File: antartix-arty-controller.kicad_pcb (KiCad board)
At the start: 2 copper layers, 68.5 x 40 mm, 103 parts, among them IC1 FT2232D, J1 QTE-020-04-L-D-A, J2 614004185023, J3 614004185023, J4 614004185023, J5 WE_629105150521, U1 PCT2075GVX, U2 PAC1934T-I_JQ, U3 USB2514B-I_M2, U4 TPS2024DR, U5 TPS2024DR, U6 TPS2024DR, U7 TPS2051BDBVR, Y1 7C-24.000MBB-T, Y2 MQ-6.000-12-30_30_

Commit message: Layout done
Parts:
- C31: moved to F.Cu
- C7, U2: moved to B.Cu
- moved N1 71.2 mm to (169.6, 89.1)
- moved C31 49.5 mm to (147.9, 61.0)
- moved N2 33.4 mm to (144.8, 72.3)
- moved C33 29.3 mm to (155.0, 61.3)
- moved C37 29.3 mm to (153.8, 61.1)
- moved U7 29.2 mm to (150.8, 60.8)
- moved D4 16.4 mm to (113.8, 77.2)
- moved R10 16.4 mm to (110.9, 80.4)
- moved R12 16.4 mm to (110.9, 77.2)
- moved D2 16.4 mm to (113.8, 80.4)
- moved D3 16.4 mm to (113.8, 82.1)
- moved D5 16.4 mm to (113.8, 78.8)
- moved R11 16.4 mm to (110.9, 82.1)
- moved R13 16.4 mm to (110.9, 78.8)
- moved C36 4.55 mm to (118.8, 77.9)
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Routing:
- net VBUS1: track 33.7 -> 16.2 mm, vias 2 -> 1
- net VBUS1_S: track 21.6 -> 4.82 mm, vias 3 -> 2
- net VBUS4_S: track 2.87 -> 15.8 mm
- net VBUS3: track 31.3 -> 29.5 mm, vias 2 -> 1
- net VBUS3_S: track 23.4 -> 22.2 mm, vias 2 -> 1
- net VBUS2_S: track 7.28 -> 8.10 mm, vias 0 -> 1
- net VBUS2: track 17.9 -> 18.6 mm, vias 0 -> 1

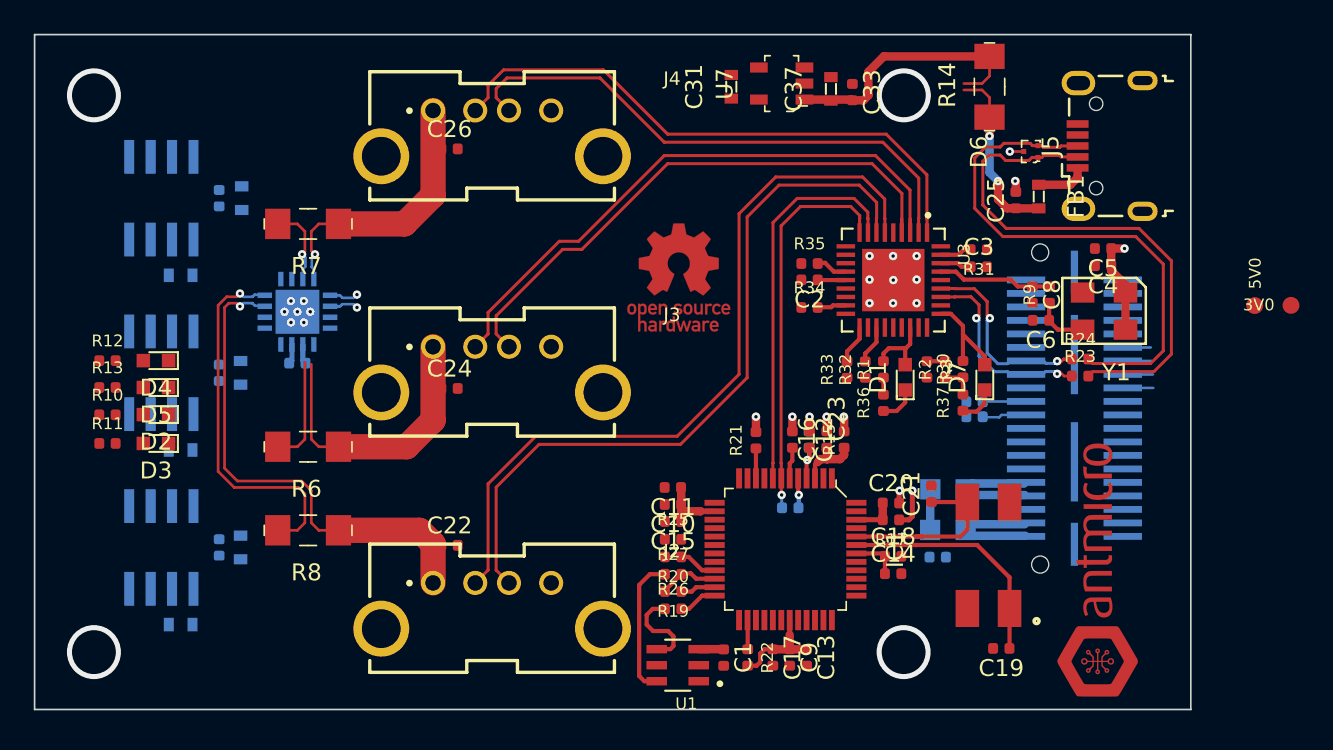
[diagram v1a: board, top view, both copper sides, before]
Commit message: Routing control signals
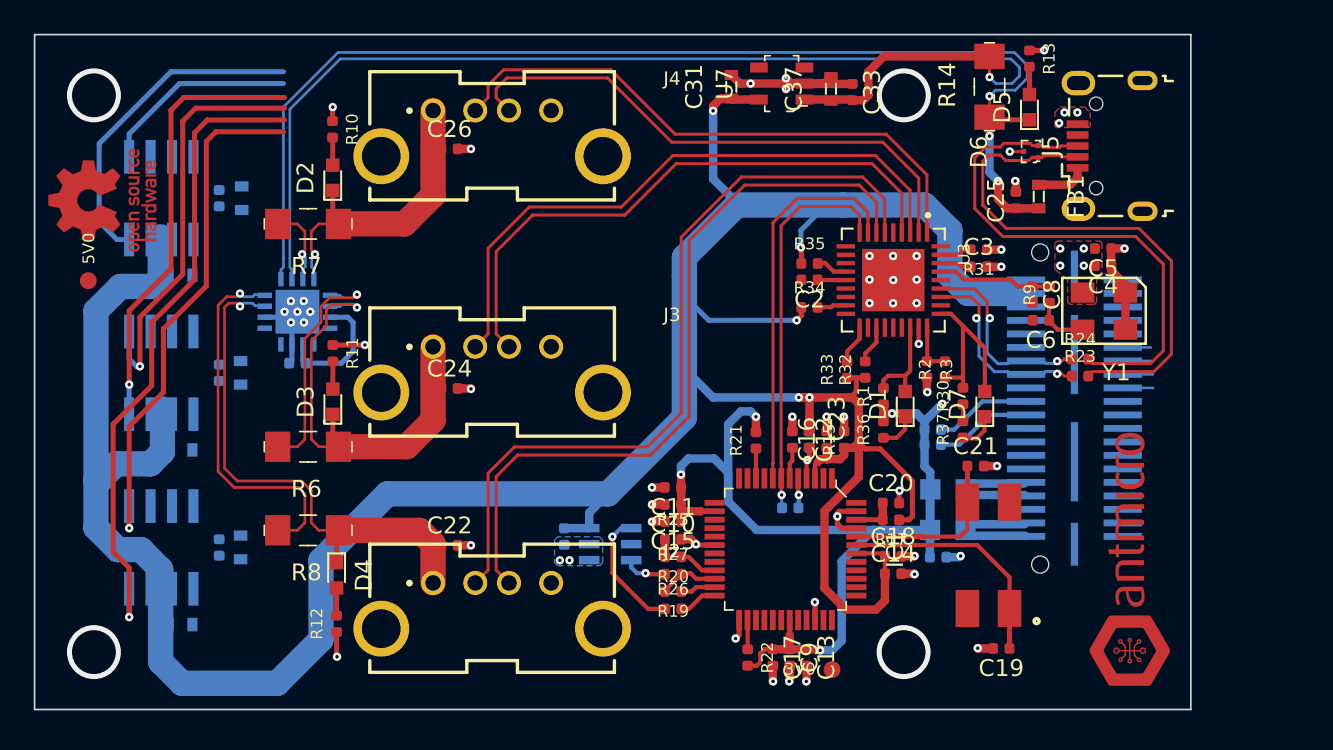
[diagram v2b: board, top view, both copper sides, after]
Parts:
- C1, U1: moved to B.Cu
- moved 5V0 69.1 mm to (109.7, 72.4)
- moved R13 58.0 mm to (165.5, 59.3), turned to 270 degrees
- moved D5 54.4 mm to (165.5, 62.2), turned to 90 degrees
- moved 3V0 34.7 mm to (153.8, 95.5)
- moved N2 34.5 mm to (110.6, 67.7), turned to 90 degrees
- moved R10 21.5 mm to (124.2, 63.5), turned to 270 degrees
- moved R12 20.7 mm to (124.5, 92.8), turned to 90 degrees
- moved D2 17.5 mm to (124.2, 66.3), turned to 90 degrees
- moved D4 16.6 mm to (124.5, 89.9), turned to 270 degrees
- moved R11 14.4 mm to (124.2, 76.7), turned to 270 degrees
- moved C1 11.9 mm to (138.0, 87.6)
- moved D3 10.8 mm to (124.2, 79.6), turned to 90 degrees
- moved U1 8.22 mm to (140.7, 88.1), turned to 0 degrees
- moved C21 3.09 mm to (162.3, 83.4), turned to 0 degrees
- moved R4 2.98 mm to (159.8, 81.3)
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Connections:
- D2 pad 1: VBUS1_S -> VBUS1
- D3 pad 1: VBUS2_S -> VBUS2
- D4 pad 1: VBUS3_S -> VBUS3
- D5 pad 1: VBUS4_S -> VBUS4
- U2 pad 17: (no net) -> GND
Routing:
- net VCC5V0: track 12.5 -> 201.7 mm, vias 2 -> 5
- net VBUS4: track 10.6 -> 70.8 mm, vias 2 -> 3
- net VBUS4_S: track 15.8 -> 72.7 mm, vias 0 -> 1
- net VCC3V3: track 22.3 -> 69.9 mm, vias 2 -> 6
- net GND: track 6.01 -> 46.1 mm, vias 15 -> 59
- net /USB3_EN: track 1.81 -> 40.2 mm, vias 0 -> 1
- net /OC_N3: track 2.31 -> 33.2 mm, vias 0 -> 1
- net /USB2_EN: track 1.79 -> 27.9 mm, vias 0 -> 1
- net /OC_N2: track 1.67 -> 26.1 mm, vias 0 -> 1
- net /USB1_EN: track 1.71 -> 21.2 mm
- net /OC_N1: track 1.85 -> 13.6 mm
- net VBUS2: track 18.6 -> 26.3 mm
- net VBUS2_S: track 8.10 -> 14.2 mm
- net SCL0: track 7.93 -> 13.2 mm, vias 0 -> 1
- net /SUSP_IND: track 6.02 -> 9.69 mm
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- added copper zone on B.Cu, net GND
- added copper zone on F.Cu, net GND
- added copper zone on In1.Cu, net GND
- added copper zone on In2.Cu, net GND
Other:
- copper layers 2 -> 4

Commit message: Board routed
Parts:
- added C40: C_1u_0402, antmicro-footprints:0402-cap, F.Cu at (165.8, 78.7)
- added C41: C_100n_0402, antartix-arty-controller-footprints:0402-cap, B.Cu at (157.5, 69.8)
- added C42: C_100n_0402, antartix-arty-controller-footprints:0402-cap, B.Cu at (160.2, 70.9)
- added C43: C_100n_0402, antartix-arty-controller-footprints:0402-cap, B.Cu at (154.9, 70.3)
- added C44: C_100n_0402, antartix-arty-controller-footprints:0402-cap, B.Cu at (160.2, 73.9)
- added C45: C_100n_0402, antartix-arty-controller-footprints:0402-cap, B.Cu at (154.9, 72.9)
- added C46: C_100n_0402, antartix-arty-controller-footprints:0402-cap, B.Cu at (157.5, 75.2)
- added C47: C_330u_KEMET_D, antmicro-footprints:KEMET_D, B.Cu at (133.7, 66.0)
- added C48: C_330u_KEMET_D, antmicro-footprints:KEMET_D, B.Cu at (133.7, 79.9)
- added C49: C_330u_KEMET_D, antmicro-footprints:KEMET_D, B.Cu at (133.7, 94.1)
- added C50: C_680u_KEMET_D, antmicro-footprints:KEMET_D, B.Cu at (123.5, 87.0)
- added GND: TP_SMD1MM, antartix-arty-controller-footprints:Testpoint_smd_1mm, F.Cu at (107.6, 74.3)
- added GND: TP_SMD1MM, antartix-arty-controller-footprints:Testpoint_smd_1mm, F.Cu at (170.7, 90.4)
- moved N1 61.5 mm to (110.2, 84.1)
- moved R4 18.7 mm to (144.4, 91.9), turned to 0 degrees
- moved R5 17.2 mm to (144.4, 89.8), turned to 180 degrees
- moved 3V0 15.3 mm to (168.2, 90.5)
- moved C26 4.93 mm to (130.1, 69.5)
- moved C24 3.94 mm to (130.1, 82.6)
- moved C36 3.22 mm to (118.3, 81.1), turned to 0 degrees
- moved R9 2.42 mm to (164.6, 74.5)
- moved C32 2.05 mm to (118.3, 79.8), turned to 0 degrees
- moved 5V0 1.88 mm to (109.3, 74.3)
- moved C4 1.14 mm to (168.8, 71.6)
- moved C5 1.14 mm to (168.8, 70.5)
- moved Y1 1.14 mm to (169.1, 74.0)
- moved C22 0.90 mm to (131.0, 87.2)
- moved D6 0.84 mm to (165.9, 64.0)
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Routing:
- net /USB1_EN: track 21.2 -> 157.3 mm, vias 0 -> 5
- net /USB2_EN: track 27.9 -> 160.6 mm, vias 1 -> 7
- net VCC3V3: track 69.9 -> 172.2 mm, vias 6 -> 15
- net /USB3_EN: track 40.2 -> 112.5 mm, vias 1 -> 3
- net SDA0: track 8.37 -> 73.2 mm, vias 1 -> 5
- net /SLOW_~ALERT: track 0.00 -> 59.6 mm, vias 0 -> 4
- net SCL0: track 13.2 -> 71.2 mm, vias 1 -> 4
- net /~PWRDN: track 0.00 -> 57.9 mm, vias 0 -> 4
- net VCC5V0: track 201.7 -> 251.2 mm, vias 5 -> 10
- net /OC_N1: track 13.6 -> 53.1 mm, vias 0 -> 5
- net /OC_N3: track 33.2 -> 68.9 mm, vias 1 -> 5
- net /OC_N2: track 26.1 -> 59.3 mm, vias 1 -> 5
- net /USB4_EN: track 0.00 -> 32.3 mm, vias 0 -> 4
- net /OC_N4: track 2.28 -> 33.1 mm, vias 0 -> 4
- net GND: track 46.1 -> 66.8 mm, vias 59 -> 95
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- added copper zone on B.Cu, net VBUS1_S
- added copper zone on B.Cu, net VBUS2_S
- added copper zone on B.Cu, net VBUS3_S
- added copper zone on F.Cu, net VCC3V3
- added copper zone on B.Cu, net VCC5V0
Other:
- board text added: "Rev. 1.0.0 02/2021"
- board text added: "Scalenode Adapter"
- board text added: "USB1"
- board text added: "USB2"
- board text added: "USB3"

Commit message: review amendments
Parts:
- removed C25: C_100n_0402, antartix-arty-controller-footprints:0402-cap
- removed C50: C_680u_KEMET_D, antmicro-footprints:KEMET_D
- removed R32: R_4k7_0402, antartix-arty-controller-footprints:0402-res
- removed U7: TPS2051BDBVR, antartix-arty-controller-footprints:SOT-753
- added J6: 0022232041, antmicro-footprints:PinHeader_1x4_P2.54mm_Drill1.02mm, F.Cu at (108.3, 65.5)
- C31: value C_100n_0603 -> C_470u_KEMET_D; footprint antmicro-footprints:0603-cap -> antartix-arty-controller-footprints:KEMET_D; moved to B.Cu
- C33: value C_100n_0402 -> C_470u_KEMET_D; footprint antartix-arty-controller-footprints:0402-cap -> antartix-arty-controller-footprints:KEMET_D; moved to B.Cu
- C37: value C_22u_0603 -> C_470u_KEMET_D; footprint antmicro-footprints:0603-cap -> antartix-arty-controller-footprints:KEMET_D; moved to B.Cu
- C47, C48: value C_330u_KEMET_D -> C_470u_KEMET_D; footprint antmicro-footprints:KEMET_D -> antartix-arty-controller-footprints:KEMET_D
- C49: value C_330u_KEMET_D -> C_100n_0402; footprint antmicro-footprints:KEMET_D -> antartix-arty-controller-footprints:0402-cap
- FB1: value BLM18PG121SN1D -> BLM21SP111BH1; footprint antartix-arty-controller-footprints:0603-res -> antartix-arty-controller-footprints:0805-res; moved to B.Cu
- R19: value R_0R_0402 -> R_220R_0402
- moved C49 48.6 mm to (170.5, 62.3), turned to 180 degrees
- moved C37 38.8 mm to (133.7, 94.3), turned to 0 degrees
- moved C33 28.4 mm to (133.7, 80.0), turned to 0 degrees
- moved N2 26.6 mm to (120.4, 92.4)
- moved C47 23.3 mm to (123.5, 87.0), turned to 90 degrees
- moved C31 15.2 mm to (133.8, 66.5), turned to 0 degrees
- moved C48 11.2 mm to (141.7, 72.1), turned to 180 degrees
- moved GND2 10.3 mm to (113.6, 65.9)
- moved 5V0 7.57 mm to (113.6, 68.1)
- moved FB1 7.33 mm to (172.4, 63.8), turned to 90 degrees
- moved R13 3.15 mm to (162.4, 59.0), turned to 0 degrees
- moved D5 2.50 mm to (164.9, 59.0), turned to 180 degrees
- moved R23 0.93 mm to (167.6, 78.1)
- moved R24 0.93 mm to (167.6, 77.1)
- moved R33 0.57 mm to (155.3, 77.7)
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- renumbered GND to GND1, GND to GND2
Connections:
- C31 pad 1: VCC5V0 -> VBUS1
- C33 pad 1: GND -> VBUS2
- C33 pad 2: VBUS4_S -> GND
- C37 pad 1: VBUS4_S -> VBUS3
- C47 pad 1: VBUS1 -> VCC5V0
- C48 pad 1: VBUS2 -> VCC5V0
- C49 pad 1: VBUS3 -> VBUS4
- R14 pad 1: VBUS4 -> VCC5V0
- R14 pad 2: VBUS4_S -> VBUS4
- R19 pad 1: Net-(IC1-Pad23) -> /SDA_FTDI
- R19 pad 2: /SDA_FTDI -> Net-(IC1-Pad23)
- U2 pad 10: VBUS4_S -> VBUS4
- U2 pad 17: GND -> (no net)
- U2 pad 9: VBUS4 -> VCC5V0
- U3 pad 20: /USB4_EN -> Net-(U3-Pad20)
- U3 pad 21: /OC_N4 -> Net-(U3-Pad21)
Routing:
- net VBUS4_S: track 73.5 -> 0.00 mm, vias 1 -> 0
- net VCC5V0: track 251.2 -> 300.6 mm, vias 10 -> 16
- net /USB3_EN: track 112.5 -> 146.1 mm, vias 3 -> 5
- net /OC_N4: track 33.1 -> 0.00 mm, vias 4 -> 0
- net /USB4_EN: track 32.3 -> 0.00 mm, vias 4 -> 0
- net VBUS4: track 71.0 -> 59.2 mm, vias 3 -> 6
- net GND: track 66.8 -> 56.5 mm, vias 95 -> 96
- net /USB2_EN: track 160.6 -> 166.2 mm
- net /OC_N1: track 53.1 -> 49.5 mm
- net Net-(FB1-Pad1): track 3.46 -> 0.00 mm, vias 0 -> 5
- net /USB1_EN: track 157.3 -> 159.5 mm, vias 5 -> 7
- net /OC_N2: track 59.3 -> 57.4 mm
- net /USB_D_CON_N: track 31.6 -> 29.8 mm
- net /USB1_D_P: track 32.6 -> 34.4 mm
- net /USB3_D_P: track 44.9 -> 46.5 mm
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- added copper zone on B.Cu, net Net-(FB1-Pad1)
- added copper zone on F.Cu, net Net-(FB1-Pad1)
- added copper zone on B.Cu, net VBUS4
- added copper zone on F.Cu, net VBUS4
- added copper zone on F.Cu, net VCC5V0
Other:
- board text added: "EN1"
- board text added: "EN2"
- board text added: "EN3"
- board text added: "GND"

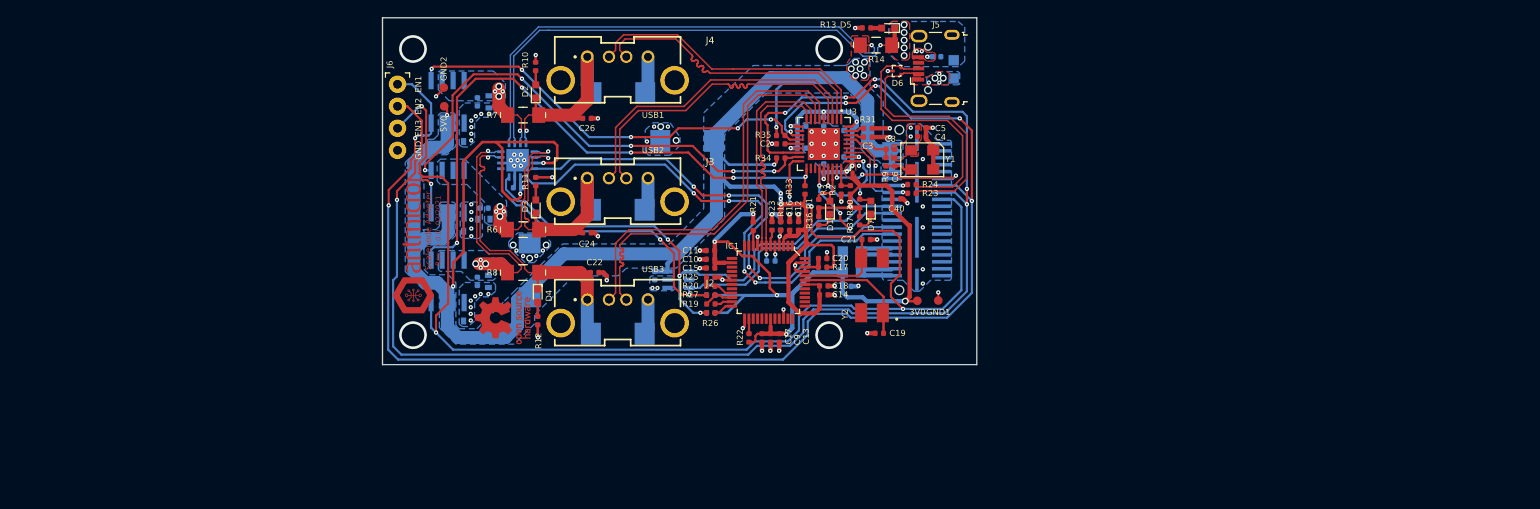
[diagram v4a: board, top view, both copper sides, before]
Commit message: Merge PCB design - Revision bumped to 1.1.0
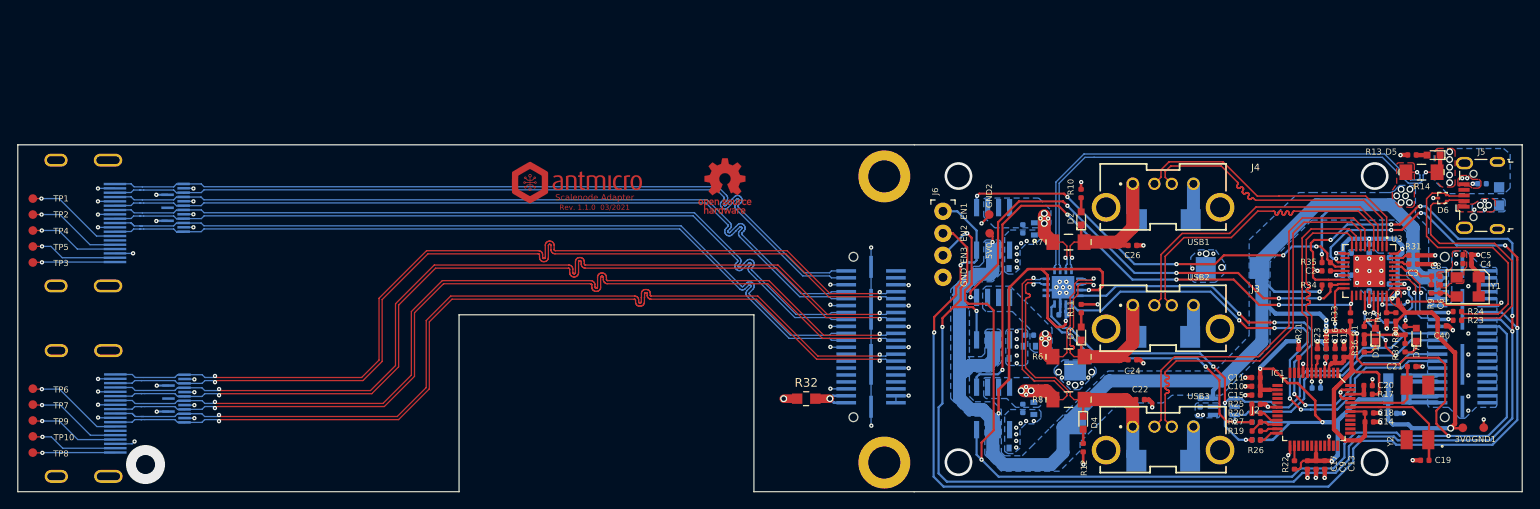
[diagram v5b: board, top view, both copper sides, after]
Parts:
- added IC2: TPD8S009DSMR, antmicro-footprints:R-PDSO-N15, B.Cu at (81.9, 79.8)
- added IC3: TPD8S009DSMR, antmicro-footprints:R-PDSO-N15, B.Cu at (82.0, 101.8)
- added J7: QTE-020-04-L-D-A, antmicro-footprints:QTE-020-04-L-D-A, B.Cu at (162.9, 94.6)
- added J8: 685119134923, antmicro-footprints:HDMI_A_Female_685119134923, B.Cu at (74.4, 81.5)
- added J9: 685119134923, antmicro-footprints:HDMI_A_Female_685119134923, B.Cu at (74.5, 103.5)
- added R32: R_0R_0805, antmicro-footprints:0805-res, F.Cu at (155.4, 101.8)
- added SP1: 9774030151, antmicro-footprints:9774030151, B.Cu at (164.4, 76.1)
- added SP2: 9774030151, antmicro-footprints:9774030151, B.Cu at (164.4, 109.1)
- added TP1: TP_SMD1MM, antmicro-footprints:Testpoint_smd_1mm, F.Cu at (66.3, 78.8)
- added TP10: TP_SMD1MM, antmicro-footprints:Testpoint_smd_1mm, F.Cu at (66.3, 106.2)
- added TP2: TP_SMD1MM, antmicro-footprints:Testpoint_smd_1mm, F.Cu at (66.3, 80.6)
- added TP3: TP_SMD1MM, antmicro-footprints:Testpoint_smd_1mm, F.Cu at (66.3, 86.1)
- added TP4: TP_SMD1MM, antmicro-footprints:Testpoint_smd_1mm, F.Cu at (66.3, 82.4)
- added TP5: TP_SMD1MM, antmicro-footprints:Testpoint_smd_1mm, F.Cu at (66.3, 84.3)
- added TP6: TP_SMD1MM, antmicro-footprints:Testpoint_smd_1mm, F.Cu at (66.3, 100.7)
- added TP7: TP_SMD1MM, antmicro-footprints:Testpoint_smd_1mm, F.Cu at (66.3, 102.5)
- added TP8: TP_SMD1MM, antmicro-footprints:Testpoint_smd_1mm, F.Cu at (66.2, 108.1)
- added TP9: TP_SMD1MM, antmicro-footprints:Testpoint_smd_1mm, F.Cu at (66.3, 104.3)
- moved D4 64.6 mm to (187.4, 104.6)
- moved R12 64.6 mm to (187.4, 107.4)
- moved 5V0 64.6 mm to (176.5, 82.7)
- moved C1 64.6 mm to (200.9, 102.3)
- moved C10 64.6 mm to (207.3, 100.4)
- moved C11 64.6 mm to (207.3, 99.3)
- moved C12 64.6 mm to (217.5, 96.5)
- moved C13 64.6 mm to (215.2, 109.4)
- moved C14 64.6 mm to (220.4, 104.5)
- moved C16 64.6 mm to (216.4, 96.5)
- moved C17 64.6 mm to (213.2, 109.4)
- moved C18 64.6 mm to (220.4, 103.4)
- moved C19 64.6 mm to (226.8, 108.9)
- moved C2 64.6 mm to (215.4, 87.0)
- moved C20 64.6 mm to (220.2, 100.3)
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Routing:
- net HDMI1_CK_P: track 0.00 -> 107.8 mm, vias 0 -> 2
- net HDMI1_CK_N: track 0.00 -> 107.2 mm, vias 0 -> 2
- net HDMI1_D1_N: track 0.00 -> 106.4 mm, vias 0 -> 2
- net HDMI1_D0_N: track 0.00 -> 106.4 mm, vias 0 -> 2
- net HDMI1_D2_N: track 0.00 -> 106.3 mm, vias 0 -> 2
- net HDMI1_D0_P: track 0.00 -> 106.3 mm, vias 0 -> 2
- net HDMI1_D1_P: track 0.00 -> 106.2 mm, vias 0 -> 2
- net HDMI1_D2_P: track 0.00 -> 106.2 mm, vias 0 -> 2
- net HDMI0_CK_N: track 0.00 -> 92.8 mm
- net HDMI0_CK_P: track 0.00 -> 92.7 mm
- net HDMI0_D2_N: track 0.00 -> 92.4 mm
- net HDMI0_D1_N: track 0.00 -> 92.4 mm
- net HDMI0_D0_N: track 0.00 -> 92.4 mm
- net HDMI0_D0_P: track 0.00 -> 92.3 mm
- net HDMI0_D1_P: track 0.00 -> 92.2 mm
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- added copper zone on In2.Cu, net VCC3V3
- removed copper zone on In2.Cu, net GND
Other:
- board size 68.5 x 40 mm -> 173.5 x 40 mm
- board text added: "Rev. 1.1.0 03/2021"
- board text removed: "Rev. 1.0.0 02/2021"
